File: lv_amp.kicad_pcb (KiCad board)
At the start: 2 copper layers, 127 x 76.2 mm, 81 parts, among them J1 Jack-DC, J2 AudioJack2, J3 AudioJack2, Q1 Q_NMOS_DGS, U1 MAX1771xSA, U2 TL072, U3 ECC83, U4 ECC83, U5 ECC83

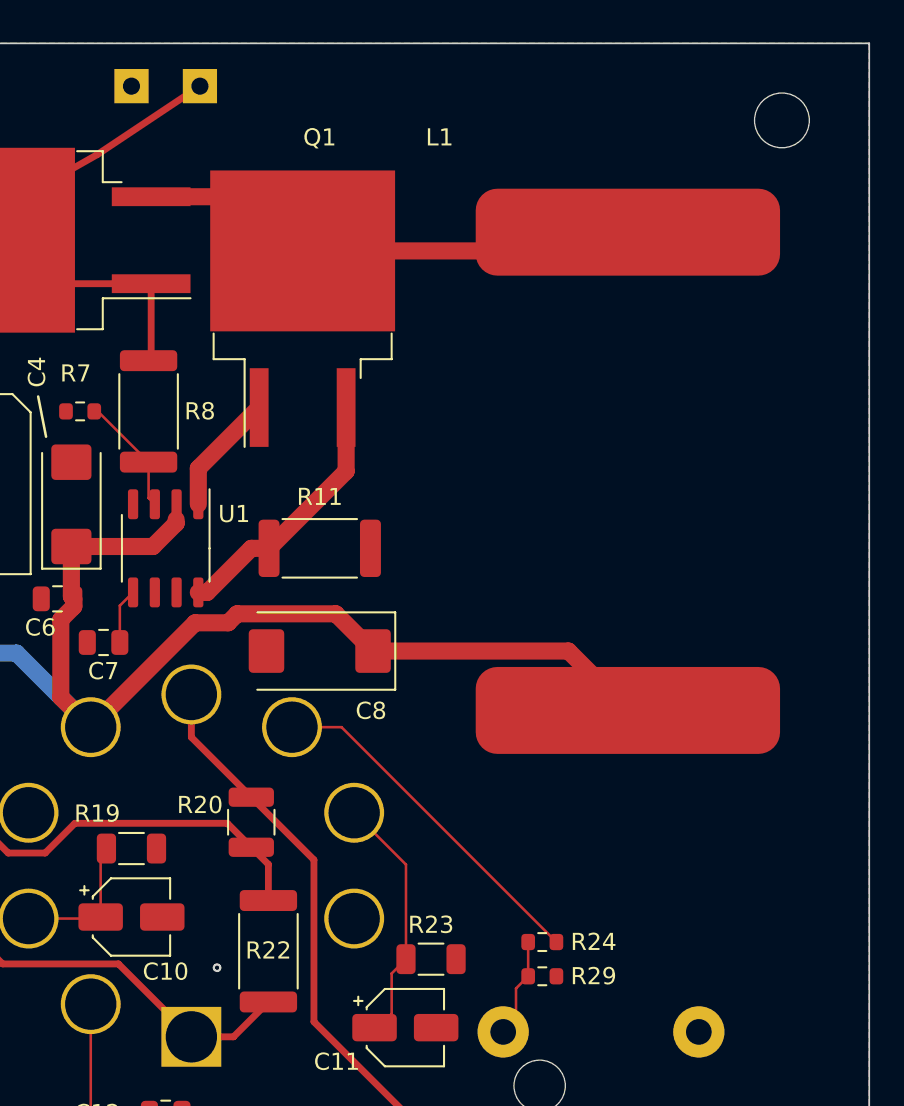
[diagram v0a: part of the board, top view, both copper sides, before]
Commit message: alpha0 errata: more input filtering on inductor
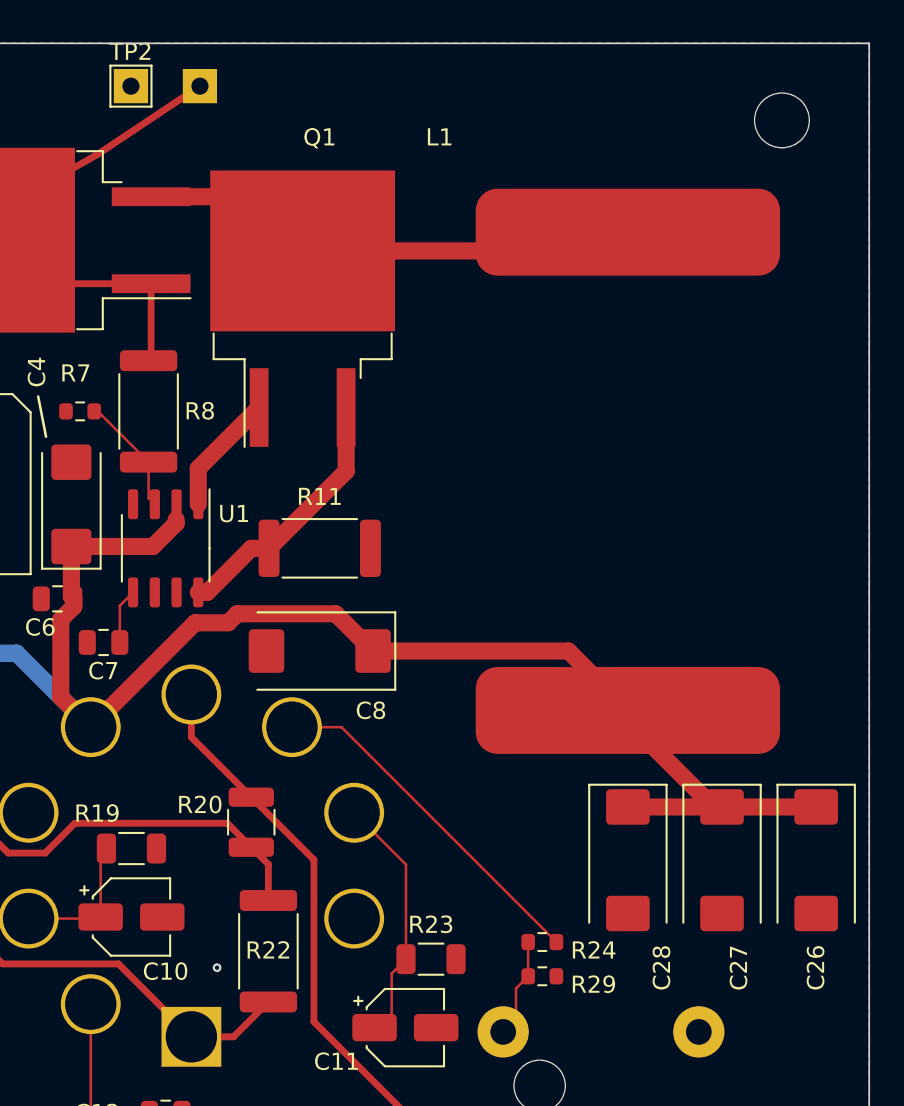
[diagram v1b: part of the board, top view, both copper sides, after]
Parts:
- added C26: 100uF, Capacitor_Tantalum_SMD:CP_EIA-7343-43_Kemet-X, F.Cu at (162.0, 111.2)
- added C27: 100uF, Capacitor_Tantalum_SMD:CP_EIA-7343-43_Kemet-X, F.Cu at (156.5, 111.2)
- added C28: 100uF, Capacitor_Tantalum_SMD:CP_EIA-7343-43_Kemet-X, F.Cu at (151.0, 111.2)
- TP2: moved to F.Cu
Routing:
- net +12V: track 204.2 -> 223.4 mm

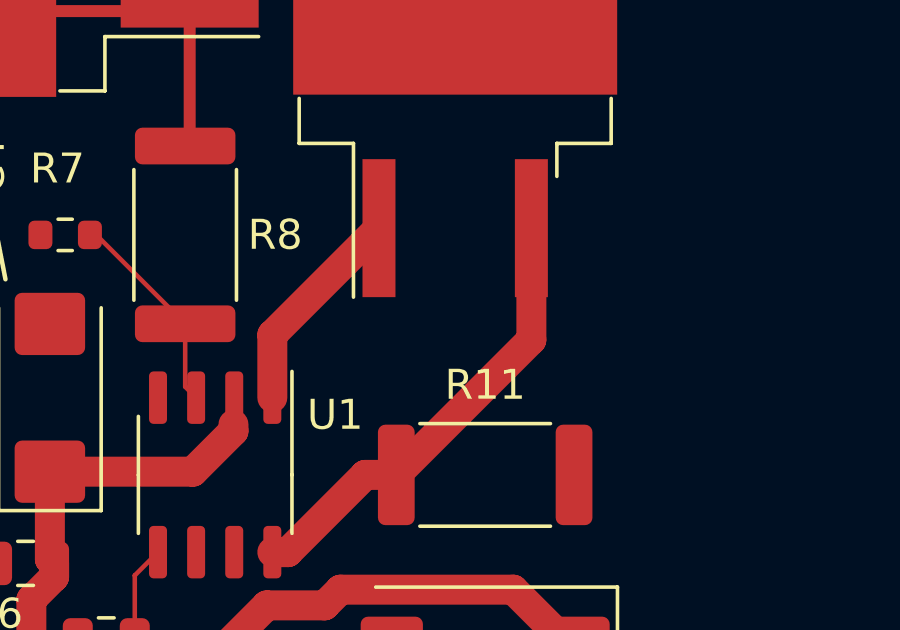
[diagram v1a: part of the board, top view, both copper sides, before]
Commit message: alpha0 errata: add gate resistor for switching mosfet
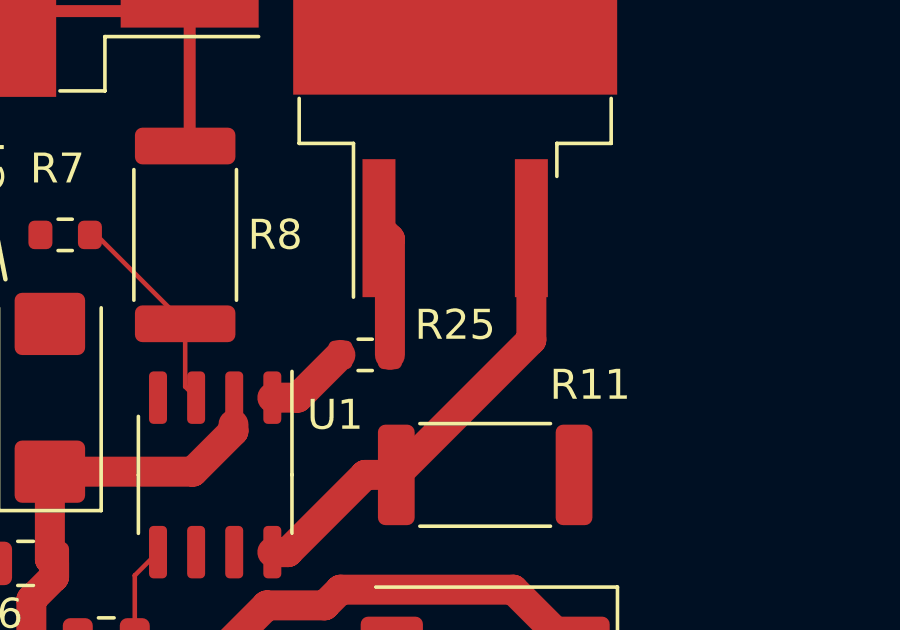
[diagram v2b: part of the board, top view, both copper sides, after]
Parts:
- added R25: 43, Resistor_SMD:R_0603_1608Metric, F.Cu at (129.0, 89.0)
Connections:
- U1 pad 1: /q1g -> /q1gr
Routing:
- net /q1gr: track 0.00 -> 2.86 mm
- net /q1g: track 7.12 -> 4.38 mm
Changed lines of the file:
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@@
   (net 53 "Net-(R33-Pad2)")
   (net 54 "unconnected-(U5-Pad9)")
+  (net 55 "/q1gr")
   (footprint "Capacitor_SMD:C_0603_1608Metric" (layer "F.Cu")
     (at 55 87 -90)
@@
     )
   )
+  (footprint "Resistor_SMD:R_0603_1608Metric" (layer "F.Cu")
+    (at 129 89)
+    (descr "Resistor SMD 0603 (1608 Metric), square (rectangular) end terminal, IPC_7351 nominal, (Body size source: IPC-SM-782 page 72, https://www.pcb-3d.com/wordpress/wp-content/uploads/ipc-sm-782a_amendment_1_and_2.pdf), generated with kicad-footprint-generator")
+    (tags "resistor")
+    (property "Sheetfile" "lv_amp.kicad_sch")
+    (property "Sheetname" "")
+    (attr smd)
+    (fp_text reference "R25" (at 3 -1) (layer "F.SilkS")
+      (effects (font (size 1 1) (thickness 0.15)))
+    )
+    (fp_text value "43" (at 0 1.43) (layer "F.Fab")
+      (effects (font (size 1 1) (thickness 0.15)))
+    )
+    (fp_text user "${REFERENCE}" (at 0 0) (layer "F.Fab")
+      (effects (font (size 0.4 0.4) (thickness 0.06)))
+    )
+    (fp_line (start -0.237258 0.5225) (end 0.237258 0.5225) (layer "F.SilkS") (width 0.12))
+    (fp_line (start -0.237258 -0.5225) (end 0.237258 -0.5225) (layer "F.SilkS") (width 0.12))
+    (fp_line (start -1.48 -0.73) (end 1.48 -0.73) (layer "F.CrtYd") (width 0.05))
+    (fp_line (start -1.48 0.73) (end -1.48 -0.73) (layer "F.CrtYd") (width 0.05))
+    (fp_line (start 1.48 0.73) (end -1.48 0.73) (layer "F.CrtYd") (width 0.05))
+    (fp_line (start 1.48 -0.73) (end 1.48 0.73) (layer "F.CrtYd") (width 0.05))
+    (fp_line (start 0.8 -0.4125) (end 0.8 0.4125) (layer "F.Fab") (width 0.1))
+    (fp_line (start 0.8 0.4125) (end -0.8 0.4125) (layer "F.Fab") (width 0.1))
+    (fp_line (start -0.8 -0.4125) (end 0.8 -0.4125) (layer "F.Fab") (width 0.1))
+    (fp_line (start -0.8 0.4125) (end -0.8 -0.4125) (layer "F.Fab") (width 0.1))
+    (pad "1" smd roundrect locked (at -0.825 0) (size 0.8 0.95) (layers "F.Cu" "F.Paste" "F.Mask") (roundrect_rratio 0.25)
+      (net 55 "/q1gr") (pintype "passive"))
+    (pad "2" smd roundrect locked (at 0.825 0) (size 0.8 0.95) (layers "F.Cu" "F.Paste" "F.Mask") (roundrect_rratio 0.25)
+      (net 52 "/q1g") (pintype "passive"))
+    (model "${KICAD6_3DMODEL_DIR}/Resistor_SMD.3dshapes/R_0603_1608Metric.wrl"
+      (offset (xyz 0 0 0))
+      (scale (xyz 1 1 1))
+      (rotate (xyz 0 0 0))
+    )
+  )
   (footprint "Resistor_SMD:R_1206_3216Metric" (layer "F.Cu")
     (at 122 110.5375)
@@
     (fp_line (start -1.95 -1.475) (end -0.975 -2.45) (layer "F.Fab") (width 0.1))
     (pad "1" smd roundrect locked (at -2.575 -1.905 270) (size 1.75 0.6) (layers "F.Cu" "F.Paste" "F.Mask") (roundrect_rratio 0.25)
-      (net 52 "/q1g") (pinfunction "EXT") (pintype "output"))
+      (net 55 "/q1gr") (pinfunction "EXT") (pintype "output"))
     (pad "2" smd roundrect locked (at -2.575 -0.635 270) (size 1.75 0.6) (layers "F.Cu" "F.Paste" "F.Mask") (roundrect_rratio 0.25)
       (net 17 "+12V") (pinfunction "V+") (pintype "power_in"))
@@
     (property "Sheetname" "")
     (attr smd)
-    (fp_text reference "R11" (at 0 -3) (layer "F.SilkS")
+    (fp_text reference "R11" (at 3.5 -3) (layer "F.SilkS")
       (effects (font (size 1 1) (thickness 0.15)))
     )
@@
   (segment (start 49.765 116.305) (end 49.765 121.455) (width 0.1524) (layer "F.Cu") (net 49))
   (segment (start 48.495 116.305) (end 49.765 116.305) (width 0.1524) (layer "F.Cu") (net 49))
-  (segment (start 125.905 90.425) (end 125.905 88.33) (width 1) (layer "F.Cu") (net 52))
-  (segment (start 125.905 88.33) (end 129.46 84.775) (width 1) (layer "F.Cu") (net 52))
+  (segment (start 129.825 85.14) (end 129.46 84.775) (width 1) (layer "F.Cu") (net 52))
+  (segment (start 129.825 89) (end 129.825 85.14) (width 1) (layer "F.Cu") (net 52))
   (segment (start 122.0375 131.5) (end 119.622148 129.084648) (width 0.1524) (layer "F.Cu") (net 53))
   (segment (start 119.622148 129.084648) (end 119.622148 119.627669) (width 0.1524) (layer "F.Cu") (net 53))
+  (segment (start 126.75 90.425) (end 128.175 89) (width 1) (layer "F.Cu") (net 55))
+  (segment (start 125.905 90.425) (end 126.75 90.425) (width 1) (layer "F.Cu") (net 55))
   (zone (net 9) (net_name "GND") (layers F&B.Cu) (hatch edge 0.508)
     (connect_pads (clearance 0.508))

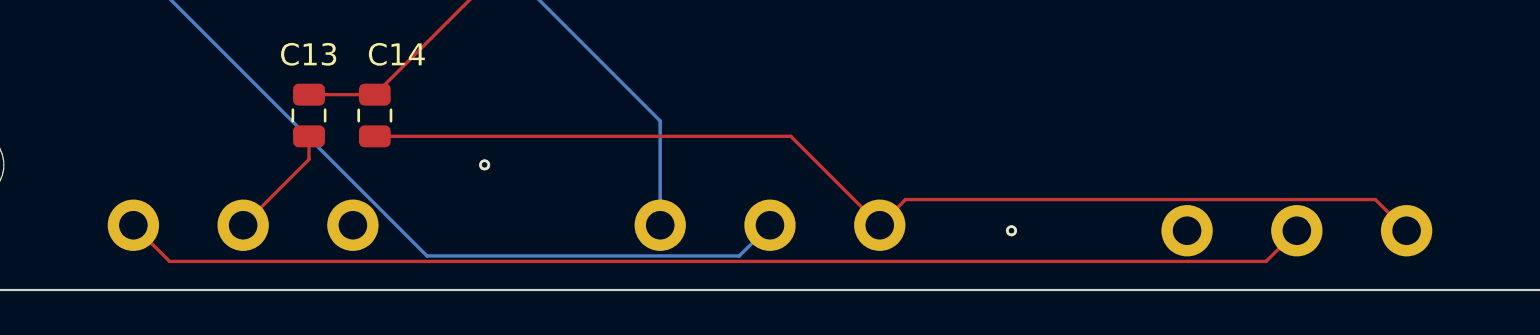
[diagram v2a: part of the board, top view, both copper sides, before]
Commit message: alpha0 errata: flip mid pot
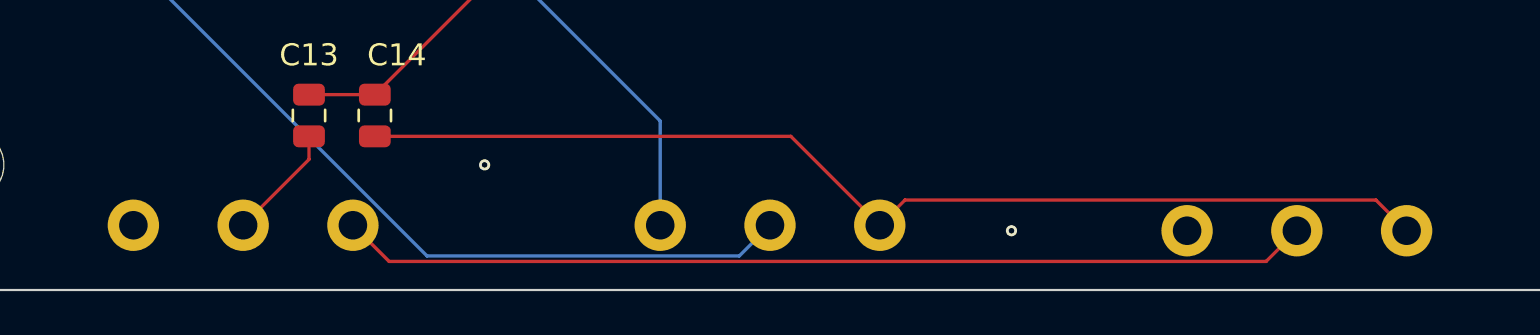
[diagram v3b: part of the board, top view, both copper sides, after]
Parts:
- RV1: value 500k -> 500k Audio
- RV2: value 1meg -> 1meg Audio
- RV3: value 500k -> 500k Linear
- RV4: value 25k -> 25k Linear
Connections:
- RV4 pad 1: GND -> Net-(RV2-Pad2)
- RV4 pad 3: Net-(RV2-Pad2) -> GND
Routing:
- net Net-(RV2-Pad2): track 54.3 -> 44.3 mm
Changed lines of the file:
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@@
       (effects (font (size 1 1) (thickness 0.15)) (justify mirror))
     )
-    (fp_text value "1meg" (at 0 -4.25 90) (layer "B.Fab")
+    (fp_text value "1meg Audio" (at 0 -4.25 90) (layer "B.Fab")
       (effects (font (size 1 1) (thickness 0.15)) (justify mirror))
     )
@@
       (effects (font (size 1 1) (thickness 0.15)) (justify mirror))
     )
-    (fp_text value "25k" (at 0 -4.25 90) (layer "B.Fab")
+    (fp_text value "25k Linear" (at 0 -4.25 90) (layer "B.Fab")
       (effects (font (size 1 1) (thickness 0.15)) (justify mirror))
     )
@@
     (fp_line (start 1.5 1.5) (end 6.5 1.5) (layer "B.Fab") (width 0.1))
     (pad "1" thru_hole circle locked (at 0 0 270) (size 2.34 2.34) (drill 1.3) (layers *.Cu *.Mask)
-      (net 9 "GND") (pinfunction "1") (pintype "passive"))
+      (net 48 "Net-(RV2-Pad2)") (pinfunction "1") (pintype "passive"))
     (pad "2" thru_hole circle locked (at 0 5 270) (size 2.34 2.34) (drill 1.3) (layers *.Cu *.Mask)
       (net 11 "Net-(C13-Pad2)") (pinfunction "2") (pintype "passive"))
     (pad "3" thru_hole circle locked (at 0 10 270) (size 2.34 2.34) (drill 1.3) (layers *.Cu *.Mask)
-      (net 48 "Net-(RV2-Pad2)") (pinfunction "3") (pintype "passive"))
+      (net 9 "GND") (pinfunction "3") (pintype "passive"))
     (model "${KICAD6_3DMODEL_DIR}/Potentiometer_THT.3dshapes/Potentiometer_Piher_T-16H_Single_Horizontal.wrl"
       (offset (xyz 0 0 0))
@@
       (effects (font (size 1 1) (thickness 0.15)) (justify mirror))
     )
-    (fp_text value "500k" (at 0 -4.25 90) (layer "B.Fab")
+    (fp_text value "500k Audio" (at 0 -4.25 90) (layer "B.Fab")
       (effects (font (size 1 1) (thickness 0.15)) (justify mirror))
     )
@@
       (effects (font (size 1 1) (thickness 0.15)) (justify mirror))
     )
-    (fp_text value "500k" (at 0 -4.25 90) (layer "B.Fab")
+    (fp_text value "500k Linear" (at 0 -4.25 90) (layer "B.Fab")
       (effects (font (size 1 1) (thickness 0.15)) (justify mirror))
     )
@@
   (segment (start 57.49376 87.19688) (end 58.29688 88) (width 0.1524) (layer "F.Cu") (net 4))
   (via (at 66 124) (size 0.508) (drill 0.254) (layers "F.Cu" "B.Cu") (net 4))
+  (segment (start 74 132) (end 66 124) (width 0.1524) (layer "B.Cu") (net 4))
   (segment (start 74 136.75) (end 74 132) (width 0.1524) (layer "B.Cu") (net 4))
-  (segment (start 74 132) (end 66 124) (width 0.1524) (layer "B.Cu") (net 4))
   (segment (start 137.2 117.8375) (end 138.0375 117) (width 0.1524) (layer "F.Cu") (net 5))
   (segment (start 138.0375 111.474266) (end 135.010565 108.447331) (width 0.1524) (layer "F.Cu") (net 5))
@@
   (segment (start 55 136.75) (end 58 133.75) (width 0.1524) (layer "F.Cu") (net 11))
   (segment (start 58 133.75) (end 58 132.7) (width 0.1524) (layer "F.Cu") (net 11))
+  (segment (start 108 137) (end 106.601889 135.601889) (width 0.1524) (layer "F.Cu") (net 12))
+  (segment (start 85.148111 135.601889) (end 84 136.75) (width 0.1524) (layer "F.Cu") (net 12))
+  (segment (start 106.601889 135.601889) (end 85.148111 135.601889) (width 0.1524) (layer "F.Cu") (net 12))
+  (segment (start 84 136.75) (end 79.95 132.7) (width 0.1524) (layer "F.Cu") (net 12))
   (segment (start 79.95 132.7) (end 61 132.7) (width 0.1524) (layer "F.Cu") (net 12))
-  (segment (start 85.169999 135.580001) (end 106.580001 135.580001) (width 0.1524) (layer "F.Cu") (net 12))
-  (segment (start 84 136.75) (end 85.169999 135.580001) (width 0.1524) (layer "F.Cu") (net 12))
-  (segment (start 106.580001 135.580001) (end 108 137) (width 0.1524) (layer "F.Cu") (net 12))
-  (segment (start 84 136.75) (end 79.95 132.7) (width 0.1524) (layer "F.Cu") (net 12))
   (segment (start 124.9625 133.4375) (end 124.9625 131.5) (width 0.1524) (layer "F.Cu") (net 13))
   (segment (start 124.4 134) (end 124.4 134.15) (width 0.1524) (layer "F.Cu") (net 13))
@@
   (segment (start 76.420396 74) (end 71.909831 69.489435) (width 0.4) (layer "F.Cu") (net 46))
   (segment (start 76.9625 74) (end 76.420396 74) (width 0.4) (layer "F.Cu") (net 46))
-  (segment (start 101.601889 138.398111) (end 103 137) (width 0.1524) (layer "F.Cu") (net 48))
-  (segment (start 51.648111 138.398111) (end 101.601889 138.398111) (width 0.1524) (layer "F.Cu") (net 48))
-  (segment (start 50 136.75) (end 51.648111 138.398111) (width 0.1524) (layer "F.Cu") (net 48))
+  (segment (start 101.601889 138.398111) (end 61.648111 138.398111) (width 0.1524) (layer "F.Cu") (net 48))
+  (segment (start 61.648111 138.398111) (end 60 136.75) (width 0.1524) (layer "F.Cu") (net 48))
+  (segment (start 103 137) (end 101.601889 138.398111) (width 0.1524) (layer "F.Cu") (net 48))
   (segment (start 49.765 116.305) (end 49.765 121.455) (width 0.1524) (layer "F.Cu") (net 49))
   (segment (start 48.495 116.305) (end 49.765 116.305) (width 0.1524) (layer "F.Cu") (net 49))

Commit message: alpha0 errata: reduce R18 to reduce stage 4 gain
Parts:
- R18: value 1Meg -> 100k
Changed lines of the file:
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@@
       (effects (font (size 1 1) (thickness 0.15)))
     )
-    (fp_text value "1Meg" (at 0 1.43) (layer "F.Fab")
+    (fp_text value "100k" (at 0 1.43) (layer "F.Fab")
       (effects (font (size 1 1) (thickness 0.15)))
     )

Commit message: alpha0 errata: increase r1 to 4.3k to increase output level
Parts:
- R1: value 1k -> 4.3k
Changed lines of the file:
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@@
       (effects (font (size 1 1) (thickness 0.15)))
     )
-    (fp_text value "1k" (at 0 1.43 90) (layer "F.Fab")
+    (fp_text value "4.3k" (at 0 1.43 90) (layer "F.Fab")
       (effects (font (size 1 1) (thickness 0.15)))
     )

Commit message: alpha0 errata: decrease r12 to 27k to reduce stage 5 gain
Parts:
- R12: value 56k -> 27k
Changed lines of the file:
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@@
       (effects (font (size 1 1) (thickness 0.15)))
     )
-    (fp_text value "56k" (at 0 2.62) (layer "F.Fab")
+    (fp_text value "27k" (at 0 2.62) (layer "F.Fab")
       (effects (font (size 1 1) (thickness 0.15)))
     )
